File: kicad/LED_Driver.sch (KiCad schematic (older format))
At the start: 24 parts, among them Q401 IRLML2502, Q402 IRLML2502, Q403 IRLML2502

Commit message: Started assigning foot prints to the parts
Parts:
- D401: renamed from D404; footprint (none) -> LEDs:LED_0805
- D402: renamed from D405; footprint (none) -> LEDs:LED_0805
- D403: renamed from D406; footprint (none) -> LEDs:LED_0805
- D404: renamed from D401; value D -> 1N4148W; Conrad-PN (none) -> N/A; Digikey-PN (none) -> 1N4148WFL-G3-08GICT-ND; MFP (none) -> 1N4148WFL-G3-08
- D405: renamed from D402; value D -> 1N4148W; Conrad-PN (none) -> N/A; Digikey-PN (none) -> 1N4148WFL-G3-08GICT-ND; MFP (none) -> 1N4148WFL-G3-08
- D406: renamed from D403; value D -> 1N4148W; Conrad-PN (none) -> N/A; Digikey-PN (none) -> 1N4148WFL-G3-08GICT-ND; MFP (none) -> 1N4148WFL-G3-08
- Q401: footprint Micro3 -> TO_SOT_Packages_SMD:SOT-23; Conrad-PN (none) -> 162827 - 62; Digikey-PN (none) -> IRLML2502GTRPBFCT-ND; MFP TPS70933DBVR -> IRLML2502GTRPBF
- Q402, Q403: footprint Micro3 -> TO_SOT_Packages_SMD:SOT-23; Conrad-PN (none) -> 162827 - 62; Digikey-PN (none) -> RLML2502GTRPBFCT-ND; MFP TPS70933DBVR -> IRLML2502GTRPBF
- R401, R402, R403, R407, R408, R409: footprint (none) -> Resistors_SMD:R_0805
- R404: renamed from R410; footprint (none) -> Resistors_SMD:R_0805
- R405, R406: renamed from R?; footprint (none) -> Resistors_SMD:R_0805
- REL101, REL102, REL103: Conrad-PN (none) -> 505000 - 62; Digikey-PN (none) -> N/A
- TP401, TP402, TP403: footprint (none) -> Measurement_Points:Measurement_Point_Round-SMD-Pad_Small

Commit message: Added more footprints to the parts
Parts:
- D404, D405, D406: footprint (none) -> Diodes_SMD:SOD-123; Conrad-PN N/A -> 564852 - 62; Digikey-PN 1N4148WFL-G3-08GICT-ND -> 1N4148W-E3-18CT-ND; MFP 1N4148WFL-G3-08 -> 1N4148W-E3-18
- REL101, REL102, REL103: footprint (none) -> tl2c-footprint:JW1AFSN-12-F
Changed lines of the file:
@@
 F 0 "REL101" H 6470 1810 60  0000 C CNN
 F 1 "Relay_UG" H 6450 2100 60  0000 C CNN
-F 2 "" H 6320 1940 60  0001 C CNN
+F 2 "tl2c-footprint:JW1AFSN-12-F" H 6320 1940 60  0001 C CNN
 F 3 "" H 6320 1940 60  0000 C CNN
 F 4 "JW1AFSN-12-F" H 6450 1950 60  0001 C CNN "MFP"
@@
 F 0 "REL102" H 6470 3610 60  0000 C CNN
 F 1 "Relay_EG" H 6450 3900 60  0000 C CNN
-F 2 "" H 6320 3740 60  0001 C CNN
+F 2 "tl2c-footprint:JW1AFSN-12-F" H 6320 3740 60  0001 C CNN
 F 3 "" H 6320 3740 60  0000 C CNN
 F 4 "JW1AFSN-12-F" H 6450 3750 60  0001 C CNN "MFP"
@@
 F 0 "REL103" H 6470 5310 60  0000 C CNN
 F 1 "Relay_OG" H 6450 5600 60  0000 C CNN
-F 2 "" H 6320 5440 60  0001 C CNN
+F 2 "tl2c-footprint:JW1AFSN-12-F" H 6320 5440 60  0001 C CNN
 F 3 "" H 6320 5440 60  0000 C CNN
 F 4 "JW1AFSN-12-F" H 6450 5450 60  0001 C CNN "MFP"
@@
 F 0 "D404" H 6425 2450 50  0000 C CNN
 F 1 "1N4148W" H 6425 2250 50  0000 C CNN
-F 2 "" H 6425 2350 50  0001 C CNN
+F 2 "Diodes_SMD:SOD-123" H 6425 2350 50  0001 C CNN
 F 3 "" H 6425 2350 50  0000 C CNN
-F 4 "1N4148WFL-G3-08 " H 6425 2350 60  0001 C CNN "MFP"
-F 5 "N/A" H 6425 2350 60  0001 C CNN "Conrad-PN"
-F 6 "1N4148WFL-G3-08GICT-ND" H 6425 2350 60  0001 C CNN "Digikey-PN"
+F 4 "1N4148W-E3-18" H 6425 2350 60  0001 C CNN "MFP"
+F 5 "564852 - 62" H 6425 2350 60  0001 C CNN "Conrad-PN"
+F 6 "1N4148W-E3-18CT-ND " H 6425 2350 60  0001 C CNN "Digikey-PN"
 	1    6425 2350
 	-1   0    0    1
@@
 F 0 "D405" H 6425 4200 50  0000 C CNN
 F 1 "1N4148W" H 6425 4000 50  0000 C CNN
-F 2 "" H 6425 4100 50  0001 C CNN
+F 2 "Diodes_SMD:SOD-123" H 6425 4100 50  0001 C CNN
 F 3 "" H 6425 4100 50  0000 C CNN
-F 4 "1N4148WFL-G3-08 " H 6425 4100 60  0001 C CNN "MFP"
-F 5 "N/A" H 6425 4100 60  0001 C CNN "Conrad-PN"
-F 6 "1N4148WFL-G3-08GICT-ND" H 6425 4100 60  0001 C CNN "Digikey-PN"
+F 4 "1N4148W-E3-18" H 6425 4100 60  0001 C CNN "MFP"
+F 5 "564852 - 62" H 6425 4100 60  0001 C CNN "Conrad-PN"
+F 6 "1N4148W-E3-18CT-ND" H 6425 4100 60  0001 C CNN "Digikey-PN"
 	1    6425 4100
 	-1   0    0    1
@@
 F 0 "D406" H 6425 5900 50  0000 C CNN
 F 1 "1N4148W" H 6425 5700 50  0000 C CNN
-F 2 "" H 6425 5800 50  0001 C CNN
+F 2 "Diodes_SMD:SOD-123" H 6425 5800 50  0001 C CNN
 F 3 "" H 6425 5800 50  0000 C CNN
-F 4 "1N4148WFL-G3-08" H 6425 5800 60  0001 C CNN "MFP"
-F 5 "N/A" H 6425 5800 60  0001 C CNN "Conrad-PN"
-F 6 "1N4148WFL-G3-08GICT-ND" H 6425 5800 60  0001 C CNN "Digikey-PN"
+F 4 "1N4148W-E3-18" H 6425 5800 60  0001 C CNN "MFP"
+F 5 "564852 - 62" H 6425 5800 60  0001 C CNN "Conrad-PN"
+F 6 "1N4148W-E3-18CT-ND" H 6425 5800 60  0001 C CNN "Digikey-PN"
 	1    6425 5800
 	-1   0    0    1

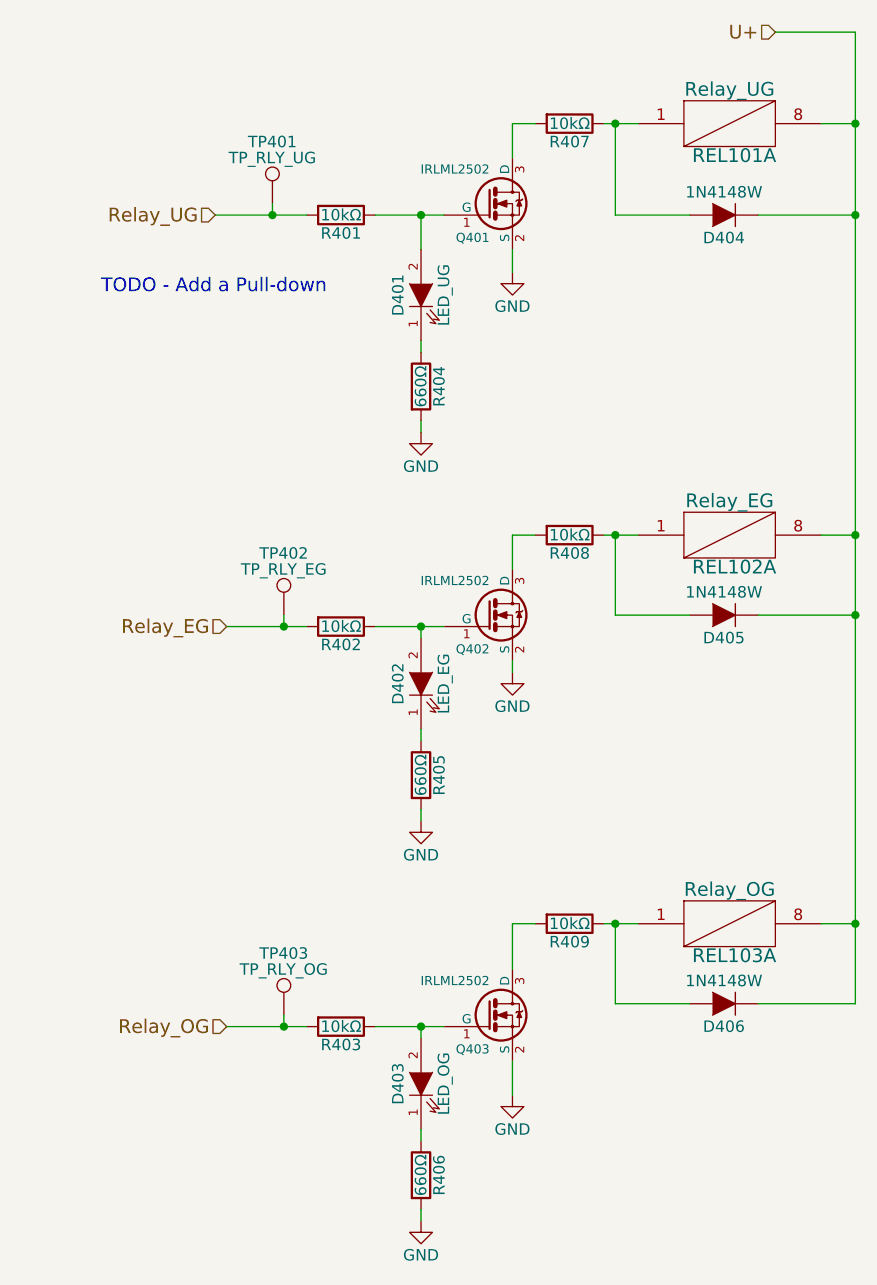
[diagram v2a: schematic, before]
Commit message: Started adding tracks to the layout
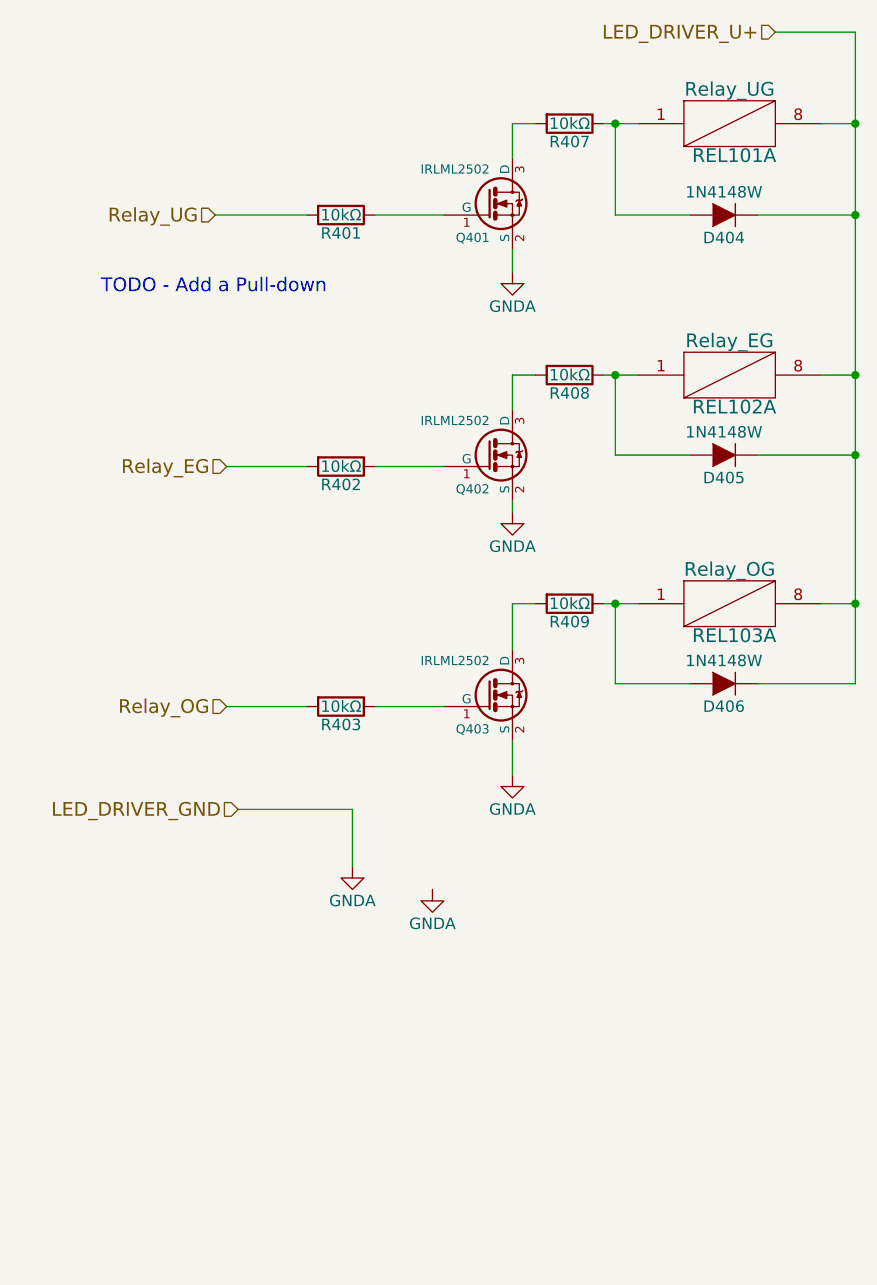
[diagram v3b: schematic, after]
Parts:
- removed D401: LED_UG, LEDs:LED_0805, symbol LED
- removed D402: LED_EG, LEDs:LED_0805, symbol LED
- removed D403: LED_OG, LEDs:LED_0805, symbol LED
- removed R404, R405, R406: 660Ω, Resistors_SMD:R_0805, symbol R
- removed TP401: TP_RLY_UG, Measurement_Points:Measurement_Point_Round-SMD-Pad_Small, symbol TEST_1P
- removed TP402: TP_RLY_EG, Measurement_Points:Measurement_Point_Round-SMD-Pad_Small, symbol TEST_1P
- removed TP403: TP_RLY_OG, Measurement_Points:Measurement_Point_Round-SMD-Pad_Small, symbol TEST_1P
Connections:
- net GND renamed GNDA
- net U+ renamed LED_DRIVER_U+
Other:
- moved on the sheet: D405, D406, Q402, Q403, R402, R403, R408, R409, REL102A, REL103A

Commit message: A change of heart with some of the parts due to sourcing
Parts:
- REL101, REL102, REL103: Conrad-PN 505000 - 62 -> 504961 - 62
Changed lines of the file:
@@
 F 3 "" H 6320 1940 60  0000 C CNN
 F 4 "JW1AFSN-12-F" H 6450 1950 60  0001 C CNN "MFP"
-F 5 "505000 - 62" H 6450 1950 60  0001 C CNN "Conrad-PN"
+F 5 "504961 - 62" H 6450 1950 60  0001 C CNN "Conrad-PN"
 F 6 "N/A" H 6450 1950 60  0001 C CNN "Digikey-PN"
 	1    6450 1950
@@
 F 3 "" H 6320 3040 60  0000 C CNN
 F 4 "JW1AFSN-12-F" H 6450 3050 60  0001 C CNN "MFP"
-F 5 "505000 - 62" H 6450 3050 60  0001 C CNN "Conrad-PN"
+F 5 "504961 - 62" H 6450 3050 60  0001 C CNN "Conrad-PN"
 F 6 "N/A" H 6450 3050 60  0001 C CNN "Digikey-PN"
 	1    6450 3050
@@
 F 3 "" H 6320 4040 60  0000 C CNN
 F 4 "JW1AFSN-12-F" H 6450 4050 60  0001 C CNN "MFP"
-F 5 "505000 - 62" H 6450 4050 60  0001 C CNN "Conrad-PN"
+F 5 "504961 - 62" H 6450 4050 60  0001 C CNN "Conrad-PN"
 F 6 "N/A" H 6450 4050 60  0001 C CNN "Digikey-PN"
 	1    6450 4050

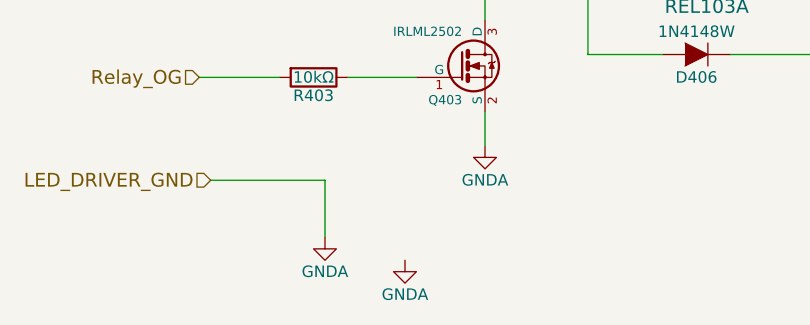
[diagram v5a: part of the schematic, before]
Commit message: Finilised the layout with a larger pin header to expose spare pins to relay driver board
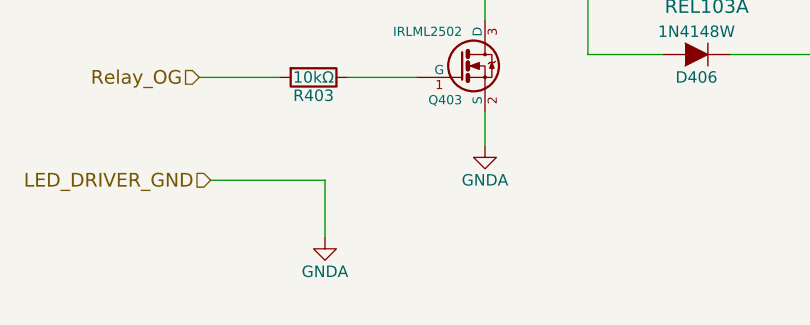
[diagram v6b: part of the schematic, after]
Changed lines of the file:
@@
 $Comp
 L GNDA #PWR029
-U 1 1 5856D981
-P 5150 5300
-F 0 "#PWR029" H 5150 5050 50  0001 C CNN
-F 1 "GNDA" H 5150 5150 50  0000 C CNN
-F 2 "" H 5150 5300 50  0000 C CNN
-F 3 "" H 5150 5300 50  0000 C CNN
-	1    5150 5300
-	1    0    0    -1
-$EndComp
-$Comp
-L GNDA #PWR030
 U 1 1 5856DA15
 P 4800 5200
-F 0 "#PWR030" H 4800 4950 50  0001 C CNN
+F 0 "#PWR029" H 4800 4950 50  0001 C CNN
 F 1 "GNDA" H 4800 5050 50  0000 C CNN
 F 2 "" H 4800 5200 50  0000 C CNN
@@
 $EndComp
 $Comp
-L GNDA #PWR031
+L GNDA #PWR030
 U 1 1 5856DA56
 P 5500 4800
-F 0 "#PWR031" H 5500 4550 50  0001 C CNN
+F 0 "#PWR030" H 5500 4550 50  0001 C CNN
 F 1 "GNDA" H 5500 4650 50  0000 C CNN
 F 2 "" H 5500 4800 50  0000 C CNN
@@
 $EndComp
 $Comp
-L GNDA #PWR032
+L GNDA #PWR031
 U 1 1 5856DA97
 P 5500 3650
-F 0 "#PWR032" H 5500 3400 50  0001 C CNN
+F 0 "#PWR031" H 5500 3400 50  0001 C CNN
 F 1 "GNDA" H 5500 3500 50  0000 C CNN
 F 2 "" H 5500 3650 50  0000 C CNN
@@
 $EndComp
 $Comp
-L GNDA #PWR033
+L GNDA #PWR032
 U 1 1 5856DAD8
 P 5500 2600
-F 0 "#PWR033" H 5500 2350 50  0001 C CNN
+F 0 "#PWR032" H 5500 2350 50  0001 C CNN
 F 1 "GNDA" H 5500 2450 50  0000 C CNN
 F 2 "" H 5500 2600 50  0000 C CNN
